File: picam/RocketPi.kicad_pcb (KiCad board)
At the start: 2 copper layers, 65 x 30 mm, 4 parts

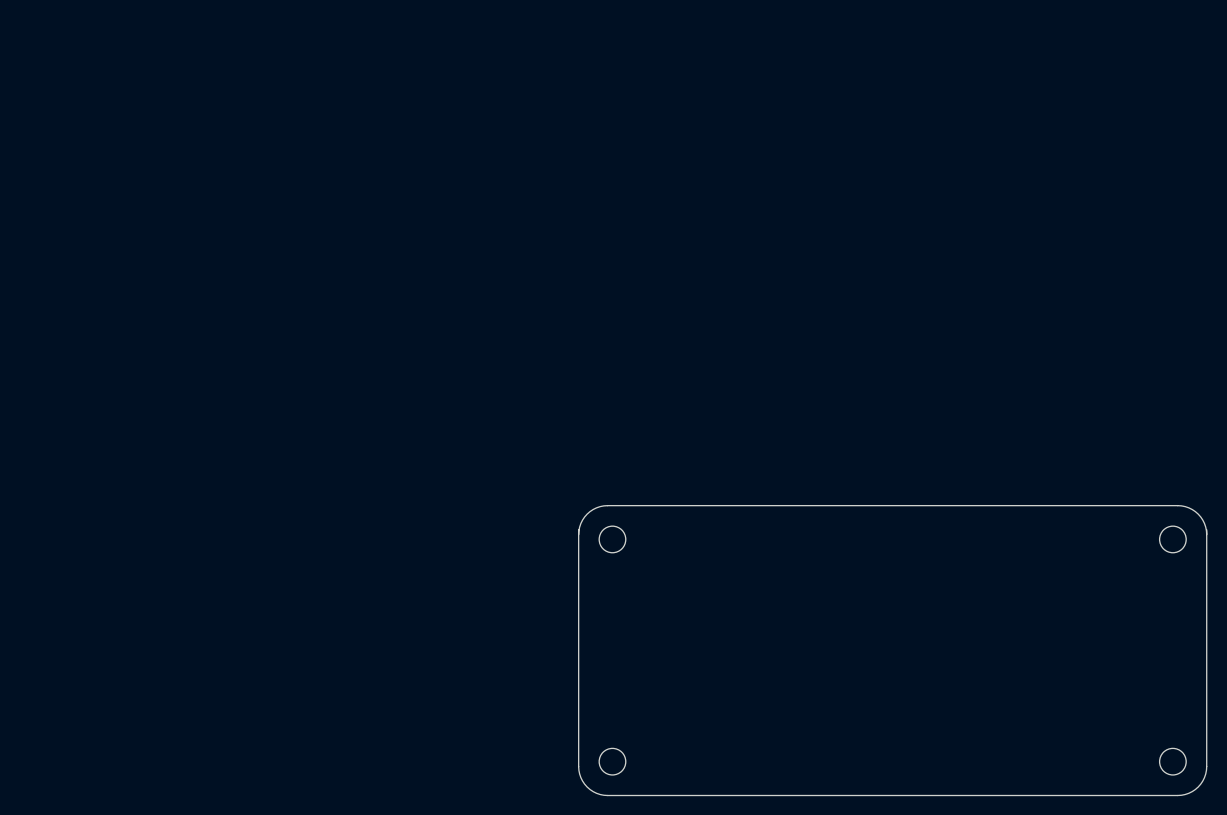
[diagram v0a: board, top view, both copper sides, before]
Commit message: Complete initial PCB layout for PiCAM board
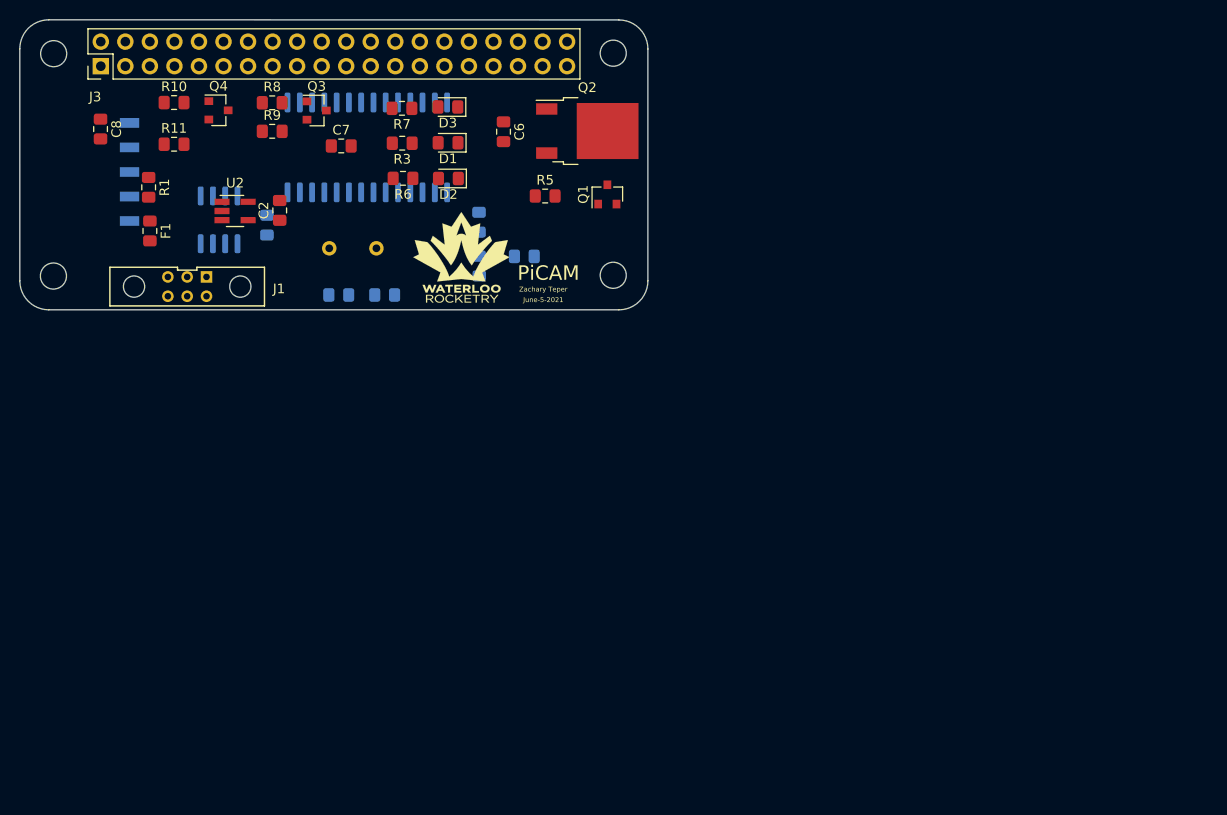
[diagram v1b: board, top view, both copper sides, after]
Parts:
- removed ? (x4): , RPi_Hat:RPi_Hat_Mounting_Hole
- added C1: 10uF, Capacitor_SMD:C_0805_2012Metric_Pad1.15x1.40mm_HandSolder, B.Cu at (90.6, 63.4)
- added C2: 100nF, Capacitor_SMD:C_0805_2012Metric_Pad1.15x1.40mm_HandSolder, F.Cu at (91.9, 61.9)
- added C3: 100nF, Capacitor_SMD:C_0805_2012Metric_Pad1.15x1.40mm_HandSolder, B.Cu at (117.3, 66.6)
- added C4: 27pF, Capacitor_SMD:C_0805_2012Metric_Pad1.15x1.40mm_HandSolder, B.Cu at (102.8, 70.6)
- added C5: 27pF, Capacitor_SMD:C_0805_2012Metric_Pad1.15x1.40mm_HandSolder, B.Cu at (98.1, 70.6)
- added C6: 100nF, Capacitor_SMD:C_0805_2012Metric_Pad1.15x1.40mm_HandSolder, F.Cu at (115.1, 53.7)
- added C7: 100nF, Capacitor_SMD:C_0805_2012Metric_Pad1.15x1.40mm_HandSolder, F.Cu at (98.3, 55.2)
- added C8: 100nF, Capacitor_SMD:C_0805_2012Metric_Pad1.15x1.40mm_HandSolder, F.Cu at (73.4, 53.5)
- added D1: Device_LED, LED_SMD:LED_0805_2012Metric_Pad1.15x1.40mm_HandSolder, F.Cu at (109.4, 54.9)
- added D2: Device_LED, LED_SMD:LED_0805_2012Metric_Pad1.15x1.40mm_HandSolder, F.Cu at (109.4, 58.6)
- added D3: Device_LED, LED_SMD:LED_0805_2012Metric_Pad1.15x1.40mm_HandSolder, F.Cu at (109.3, 51.2)
- added F1: Device_Polyfuse, Fuse:Fuse_0805_2012Metric_Pad1.15x1.40mm_HandSolder, F.Cu at (78.5, 64.0)
- added G***: LOGO, custom:rocketry_logo_small, F.Cu at (110.7, 66.8)
- added J1: CAN Communication, canhw_footprints:connector_Harwin_M80-5000642, F.Cu at (82.4, 69.8)
- added J2: Connector_Conn_01x05_Female, canhw_footprints:PinHeader_5x2.54_SMD_90deg_952-3198-1-ND, B.Cu at (76.4, 52.8)
- added J3: Conn_02x20_Counter_Clockwise_MountingPin, Connector_PinHeader_2.54mm:PinHeader_2x20_P2.54mm_Vertical, F.Cu at (73.4, 47.0)
- added M1: MountingHole_2.7mm, MountingHole:MountingHole_2.7mm, F.Cu at (68.6, 45.7)
- added M2: MountingHole_2.7mm, MountingHole:MountingHole_2.7mm, F.Cu at (68.5, 68.7)
- added M3: MountingHole_2.7mm, MountingHole:MountingHole_2.7mm, F.Cu at (126.5, 68.6)
- added M4: MountingHole_2.7mm, MountingHole:MountingHole_2.7mm, F.Cu at (126.5, 45.6)
- added Q1: BSS138, Package_TO_SOT_SMD:SOT-23, F.Cu at (125.9, 60.2)
- added Q2: AOD417, Package_TO_SOT_SMD:TO-252-2, F.Cu at (123.8, 53.7)
- added Q3: BSS138, Package_TO_SOT_SMD:SOT-23, F.Cu at (95.8, 51.6)
- added Q4: BSS138, Package_TO_SOT_SMD:SOT-23, F.Cu at (85.6, 51.5)
- added R1: 200mOhm, Resistor_SMD:R_0805_2012Metric_Pad1.15x1.40mm_HandSolder, F.Cu at (78.4, 59.5)
- added R10: 10K, Resistor_SMD:R_0805_2012Metric_Pad1.15x1.40mm_HandSolder, F.Cu at (81.0, 50.7)
- added R11: 10K, Resistor_SMD:R_0805_2012Metric_Pad1.15x1.40mm_HandSolder, F.Cu at (81.0, 55.0)
- added R2: 10K, Resistor_SMD:R_0805_2012Metric_Pad1.15x1.40mm_HandSolder, B.Cu at (112.6, 67.6)
- added R3: 330R, Resistor_SMD:R_0805_2012Metric_Pad1.15x1.40mm_HandSolder, F.Cu at (104.6, 54.9)
- added R4: 100, Resistor_SMD:R_0805_2012Metric_Pad1.15x1.40mm_HandSolder, B.Cu at (112.6, 63.1)
- added R5: 10K, Resistor_SMD:R_0805_2012Metric_Pad1.15x1.40mm_HandSolder, F.Cu at (119.4, 60.4)
- added R6: 330R, Resistor_SMD:R_0805_2012Metric_Pad1.15x1.40mm_HandSolder, F.Cu at (104.7, 58.6)
- added R7: 330R, Resistor_SMD:R_0805_2012Metric_Pad1.15x1.40mm_HandSolder, F.Cu at (104.6, 51.3)
- added R8: 10K, Resistor_SMD:R_0805_2012Metric_Pad1.15x1.40mm_HandSolder, F.Cu at (91.2, 50.8)
- added R9: 10K, Resistor_SMD:R_0805_2012Metric_Pad1.15x1.40mm_HandSolder, F.Cu at (91.2, 53.7)
- added U1: MCP2562, Package_SO:SOIC-8_3.9x4.9mm_P1.27mm, B.Cu at (85.7, 62.9)
- added U2: INA180, Package_TO_SOT_SMD:SOT-23-5_HandSoldering, F.Cu at (87.3, 62.0)
- added U3: PIC18F26K83, Package_SO:SOIC-28W_7.5x17.9mm_P1.27mm, B.Cu at (101.0, 55.4)
- added Y1: Crystal, Crystal:Crystal_HC49-U_Vertical, B.Cu at (102.0, 65.8)
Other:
- outline, holes or cut-outs redrawn
- board text added: "June-5-2021"
- board text added: "PiCAM"
- board text added: "Zachary Teper"

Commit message: Set design rules and layers for the PiCAM board
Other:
- copper layers 2 -> 4
- net class Default: via_dia 0.6 -> 0.8
- net class Power added: clearance 0.2, trace_width 0.5, via_dia 0.8, via_drill 0.4
- rule trace_min: 0.01 -> 0.2
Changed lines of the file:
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@@
   (layers
     (0 F.Cu signal)
+    (1 In1.Cu power)
+    (2 In2.Cu power)
     (31 B.Cu signal)
+    (32 B.Adhes user)
+    (33 F.Adhes user)
     (34 B.Paste user)
     (35 F.Paste user)
@@
     (40 Dwgs.User user)
     (41 Cmts.User user)
+    (42 Eco1.User user)
+    (43 Eco2.User user)
     (44 Edge.Cuts user)
+    (45 Margin user)
+    (46 B.CrtYd user)
+    (47 F.CrtYd user)
     (48 B.Fab user)
     (49 F.Fab user)
@@
   (setup
     (last_trace_width 0.25)
-    (user_trace_width 0.01)
-    (user_trace_width 0.02)
-    (user_trace_width 0.05)
-    (user_trace_width 0.1)
-    (user_trace_width 0.2)
     (trace_clearance 0.2)
     (zone_clearance 0.508)
     (zone_45_only no)
-    (trace_min 0.01)
-    (via_size 0.6)
+    (trace_min 0.2)
+    (via_size 0.8)
     (via_drill 0.4)
     (via_min_size 0.4)
@@
     (clearance 0.2)
     (trace_width 0.25)
-    (via_dia 0.6)
+    (via_dia 0.8)
     (via_drill 0.4)
     (uvia_dia 0.3)
     (uvia_drill 0.1)
     (add_net +3V3)
-    (add_net +5V)
     (add_net /CANH)
     (add_net /CANL)
@@
     (add_net /Pi_Tx)
     (add_net /pi_switching)
-    (add_net /power_pi)
     (add_net /~MCLR)
-    (add_net GND)
     (add_net "Net-(D1-Pad2)")
     (add_net "Net-(D2-Pad2)")
     (add_net "Net-(D3-Pad2)")
-    (add_net "Net-(F1-Pad1)")
-    (add_net "Net-(F1-Pad2)")
     (add_net "Net-(J1-Pad5)")
     (add_net "Net-(J3-Pad11)")
@@
     (add_net "Net-(U3-Pad7)")
   )
+  (net_class Power ""
+    (clearance 0.2)
+    (trace_width 0.5)
+    (via_dia 0.8)
+    (via_drill 0.4)
+    (uvia_dia 0.3)
+    (uvia_drill 0.1)
+    (add_net +5V)
+    (add_net /power_pi)
+    (add_net GND)
+    (add_net "Net-(F1-Pad1)")
+    (add_net "Net-(F1-Pad2)")
+  )
   (module MountingHole:MountingHole_2.7mm locked (layer F.Cu)

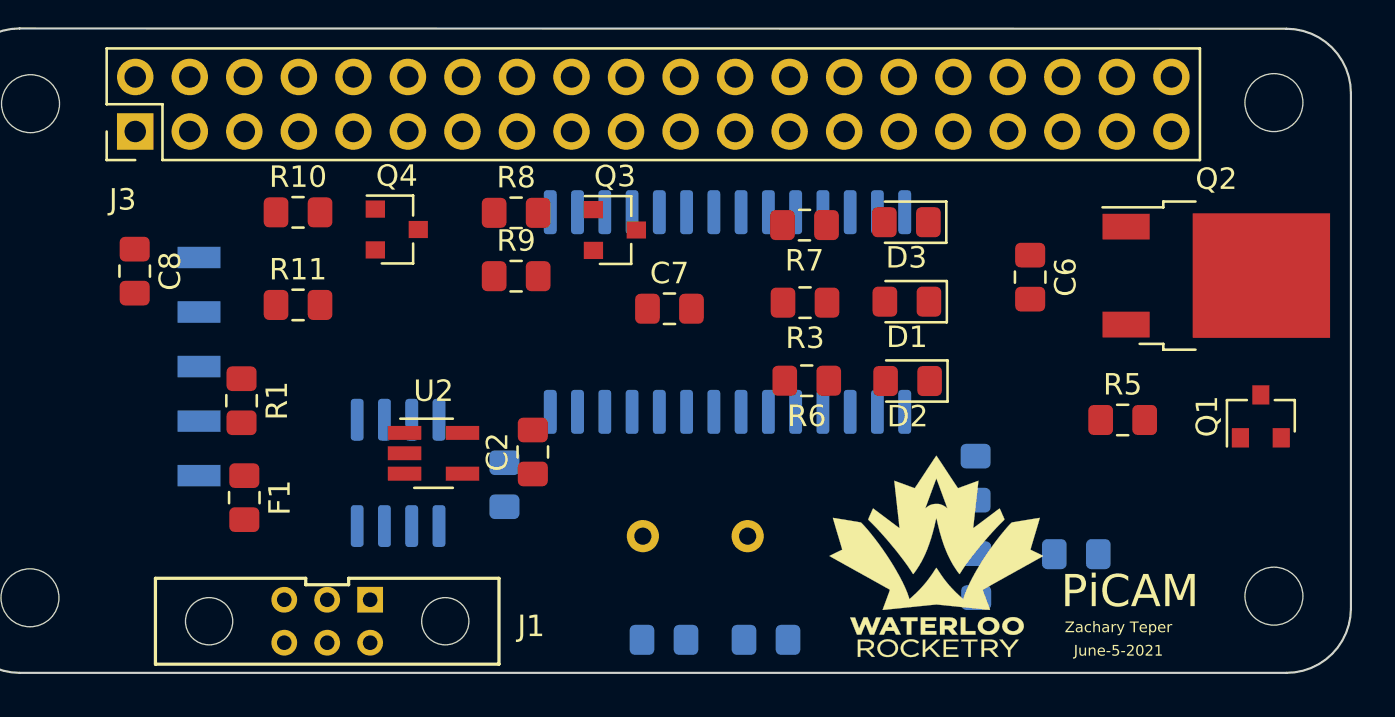
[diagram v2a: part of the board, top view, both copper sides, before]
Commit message: Route GND and +5V traces for the PiCAM board
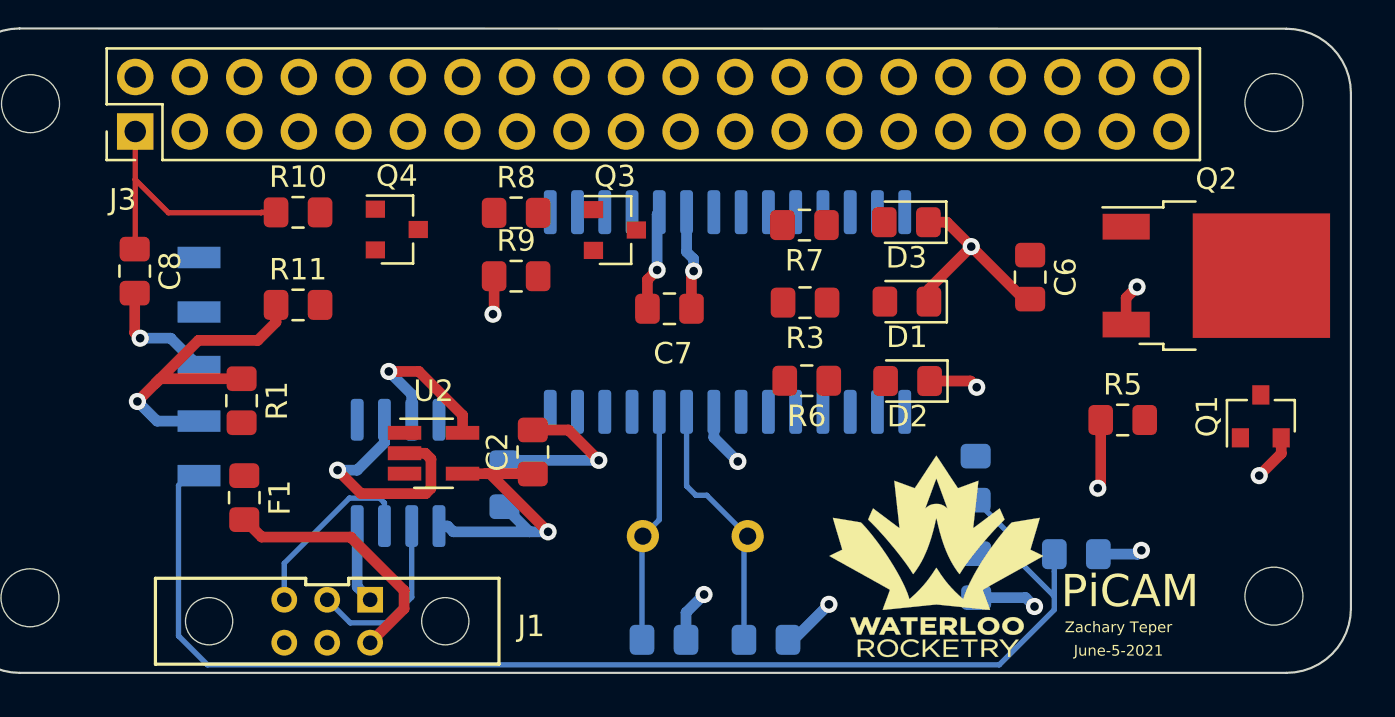
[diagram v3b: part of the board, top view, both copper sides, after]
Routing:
- net /~MCLR: track 0.00 -> 61.3 mm
- net GND: track 0.00 -> 57.4 mm, vias 0 -> 11
- net +5V: track 0.00 -> 52.6 mm, vias 0 -> 8
- net +3V3: track 0.00 -> 12.7 mm
- net /OSC1: track 0.00 -> 12.2 mm
- net Net-(F1-Pad2): track 0.00 -> 11.9 mm
- net /OSC2: track 0.00 -> 11.0 mm
- net /CANH: track 0.00 -> 8.79 mm
- net /CANL: track 0.00 -> 8.19 mm
- added copper zone on In1.Cu, net +5V
- added copper zone on In2.Cu, net GND

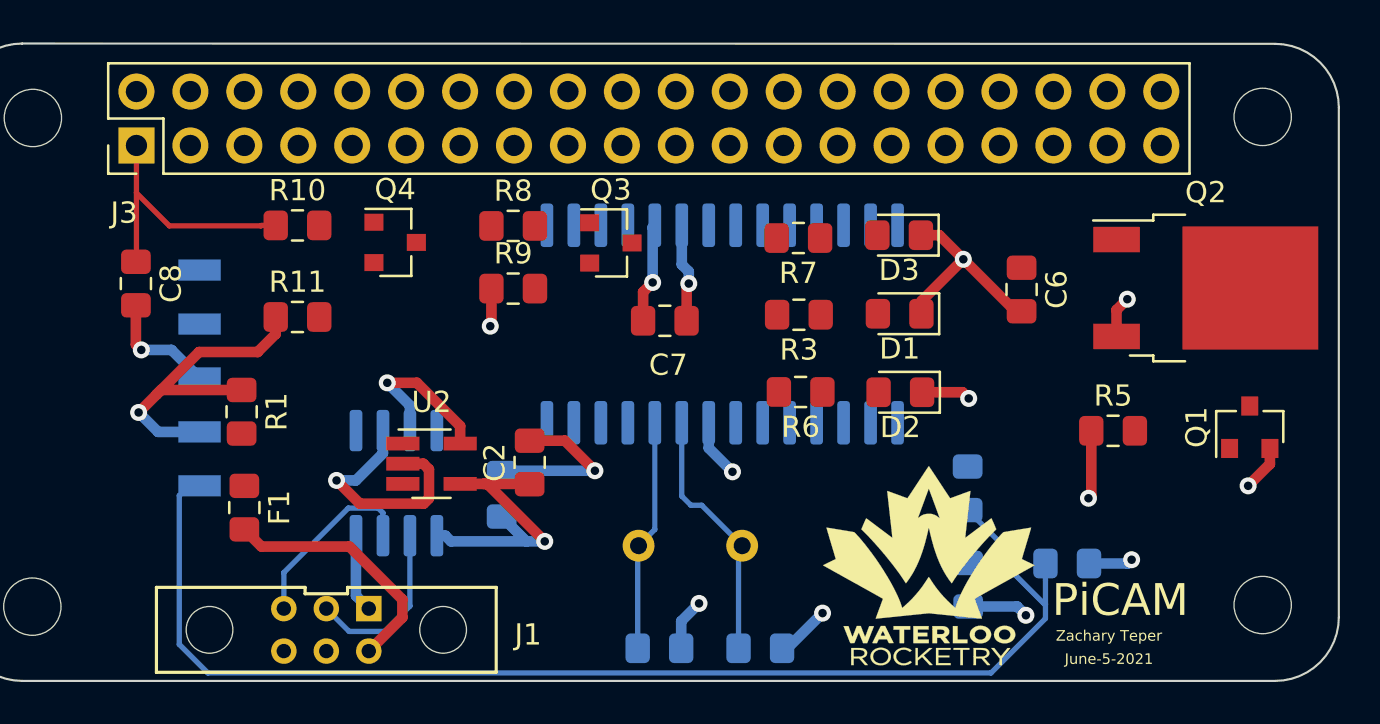
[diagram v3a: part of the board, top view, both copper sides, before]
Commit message: Finished initial PCB layout for PiCAM board
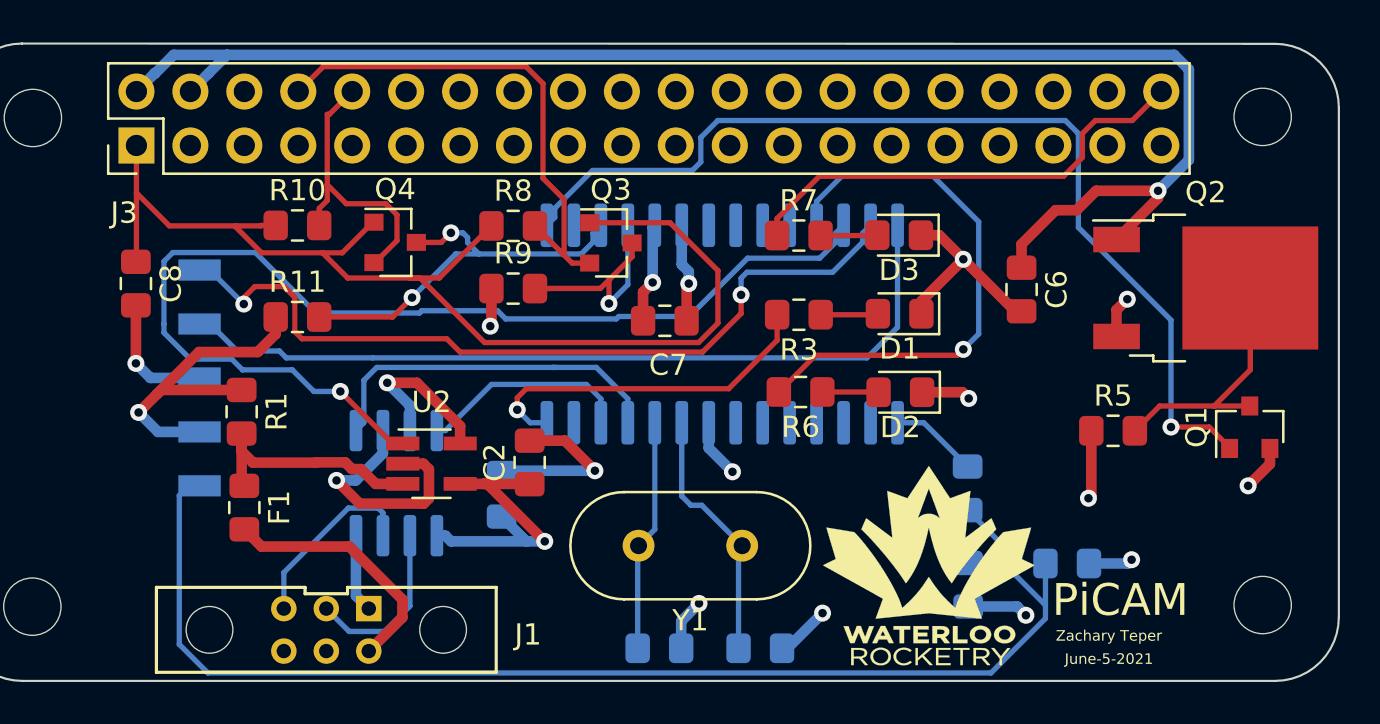
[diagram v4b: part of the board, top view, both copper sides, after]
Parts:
- Y1: moved to F.Cu
- moved R7 0.12 mm to (104.6, 51.2), turned to 0 degrees
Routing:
- net /power_pi: track 0.00 -> 71.0 mm, vias 0 -> 1
- net /CURRENT_SENSE: track 0.00 -> 52.4 mm, vias 0 -> 1
- net /pi_switching: track 0.00 -> 47.1 mm, vias 0 -> 1
- net +3V3: track 12.7 -> 55.4 mm
- net /ICSPDAT: track 0.00 -> 38.9 mm
- net /ICSPCLK: track 0.00 -> 38.7 mm, vias 0 -> 2
- net Net-(R6-Pad2): track 0.00 -> 26.0 mm, vias 0 -> 1
- net /Pi_Tx: track 0.00 -> 24.1 mm
- net Net-(J3-Pad40): track 0.00 -> 22.0 mm
- net /PIC_TX: track 0.00 -> 19.0 mm, vias 0 -> 2
- net /CAN_TX: track 0.00 -> 17.1 mm
- net Net-(R3-Pad2): track 0.00 -> 16.8 mm, vias 0 -> 1
- net /Pi_Rx: track 0.00 -> 13.6 mm
- net Net-(Q1-Pad3): track 0.00 -> 12.2 mm
- net Net-(F1-Pad1): track 0.00 -> 11.6 mm
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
